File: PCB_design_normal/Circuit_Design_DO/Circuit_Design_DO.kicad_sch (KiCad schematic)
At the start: 117 parts, among them J1 Power, J10 ICSP, J3 Analog, J4 PWM, J5 Analog, J6 COMUNICATION, J7 Digital, J8 Conn_Coaxial, J9 USB_C_Receptacle_USB2.0_16P, K1 SANYOU_SRD_Form_A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

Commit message: Outlined layout for non-Arduino PCB, started to place components
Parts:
- removed C10: 0.1u, Capacitor_SMD:C_0805_2012Metric, symbol Device:C_Polarized
- added C10: 0.1u, Capacitor_SMD:C_0805_2012Metric, symbol Device:C
- added H1, H2, H3, H4: MountingHole, MountingHole:MountingHole_3.2mm_M3_DIN965_Pad_TopBottom, symbol Mechanical:MountingHole
- SW1: value SW_Push -> Reset
- SW4: value SW_Push -> AC/DC
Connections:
- net DGND: now also C10.2
- net at D1.1 (A1), J9.A4 (VBUS), J9.A9 (VBUS)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: now also C10.1

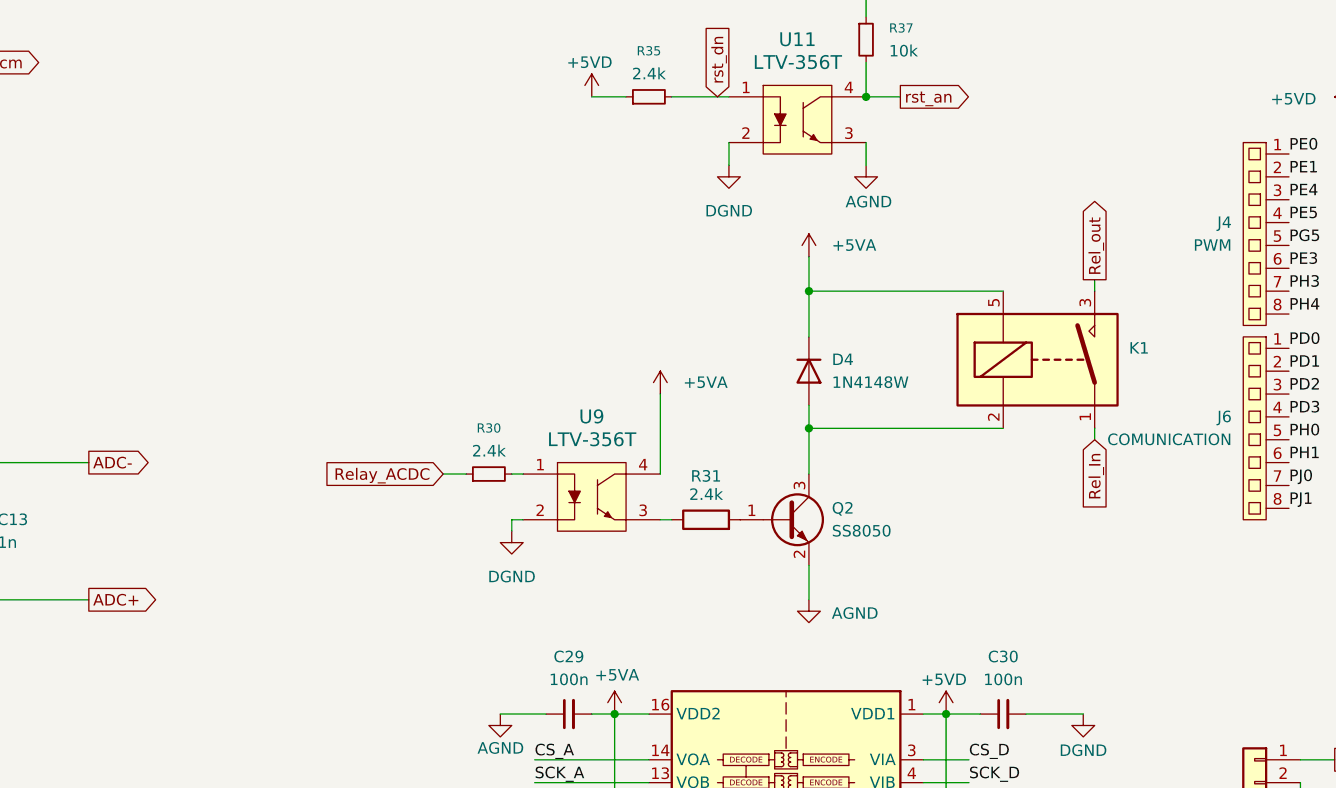
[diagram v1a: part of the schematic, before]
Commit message: Added frontend circuits, powerplanes, changed relay component
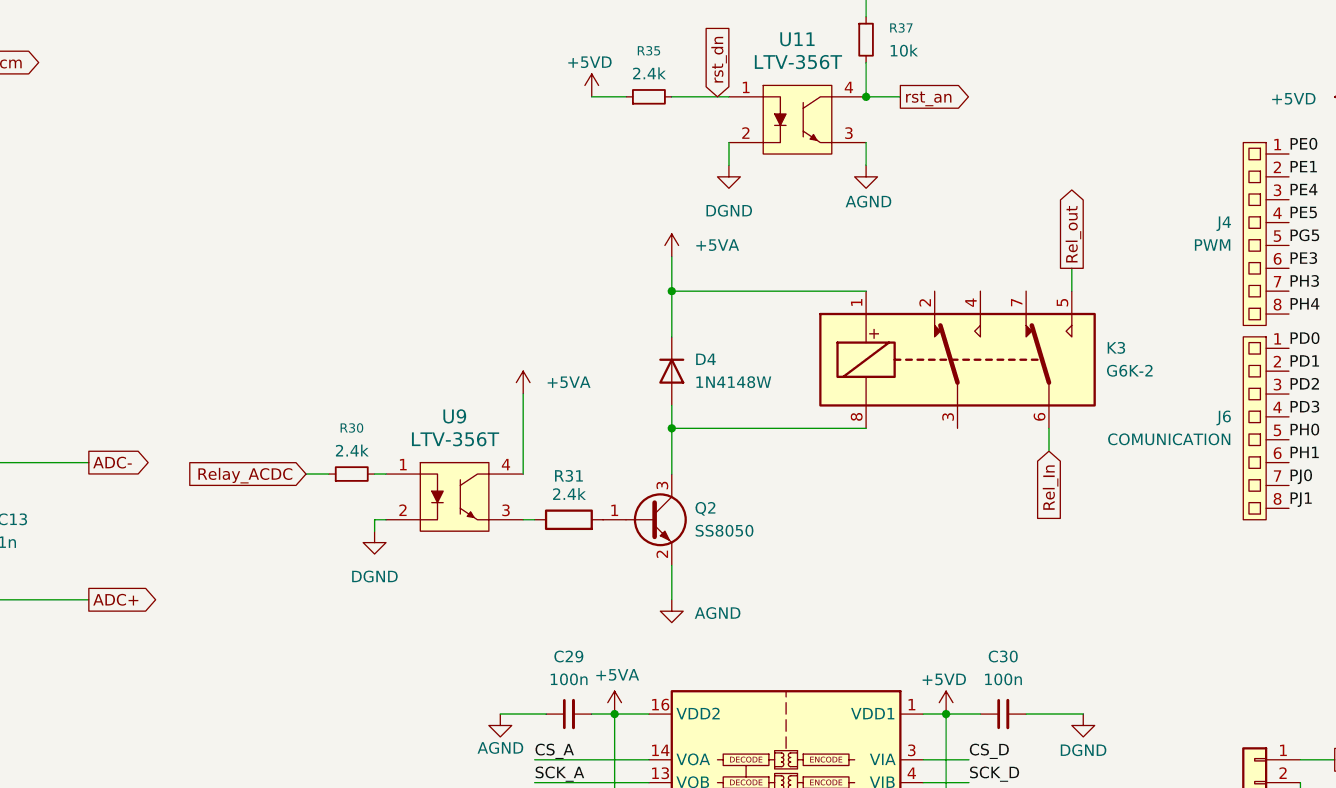
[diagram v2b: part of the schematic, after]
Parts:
- removed K1: SANYOU_SRD_Form_A, Relay_THT:Relay_SPST_SANYOU_SRD_Series_Form_A, symbol Relay:SANYOU_SRD_Form_A
- added K3: G6K-2, Relay_SMD:Relay_DPDT_Omron_G6K-2F-Y, symbol Relay:G6K-2
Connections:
- net +5VA: now also K3.1
- net Rel_In: now also K3.6
- net Rel_out: now also K3.5
- net at D4.2 (A), Q2.3 (C): now also K3.8
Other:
- moved on the sheet: D4, Q2, R30, R31, U9

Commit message: Almost done PCB design and final hardware checks
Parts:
- removed C38: 100n, Capacitor_SMD:C_0805_2012Metric, symbol Device:C_Small
- added R42: 2.4k, Resistor_SMD:R_0805_2012Metric, symbol Device:R_Small
- added R43: 10k, Resistor_SMD:R_0805_2012Metric, symbol Device:R_Small
- added U6: LTV-356T, digikey-footprints:SMD-4_4.4x3.85mm_P2.54mm, symbol dk_Optoisolators-Transistor-Photovoltaic-Output:LTV-356T
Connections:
- net PB6 is gone; now on net 10X: J2.5, U8.25 (PB6(OC1B/PCINT6))
- net +5VA: now also R43.1
- net 10X: now also R42.1; no longer J7.4 (Pin_4), U13.1, U13.5, U8.77 (PA1(AD1))
- net AGND: now also U6.3
- net CS_A: now also U4.1 (CONVST)
- net CS_D: no longer U4.1 (CONVST)
- net DGND: now also U6.2; no longer U11.2
- net rst_dn: now also U11.2; no longer R35.2, U11.1
- new net: R35.2, U11.1
- new net: R42.2, U6.1
- new net 10Xa: R43.2, U13.1, U13.5, U6.4
- new net PA1: J7.4 (Pin_4), U8.77 (PA1(AD1))
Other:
- moved on the sheet: R35, R37, U11

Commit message: Finished PCB and electronic design
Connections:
- no-connect marks 28 -> 32
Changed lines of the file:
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@@
+	)
+	(no_connect
+		(at 219.71 135.89)
 	)
 	(no_connect
@@
 	)
 	(no_connect
+		(at 222.25 120.65)
+	)
+	(no_connect
 		(at 391.16 195.58)
 	)
@@
 	)
 	(no_connect
+		(at 217.17 120.65)
+	)
+	(no_connect
 		(at 105.41 238.76)
 	)
 	(no_connect
+		(at 227.33 120.65)
+	)
+	(no_connect
